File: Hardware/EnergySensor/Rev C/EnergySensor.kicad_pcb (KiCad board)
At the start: 2 copper layers, 40 parts, among them IC1 ATMEGA328P-A, J1 JACK_3POLE, P1 MAINS, P2 CONN_02X03, P3 CONN_01X12, T1 VN20.10 09477, U1 LM1084IT-3.3/NOPB, Y1 16MHz

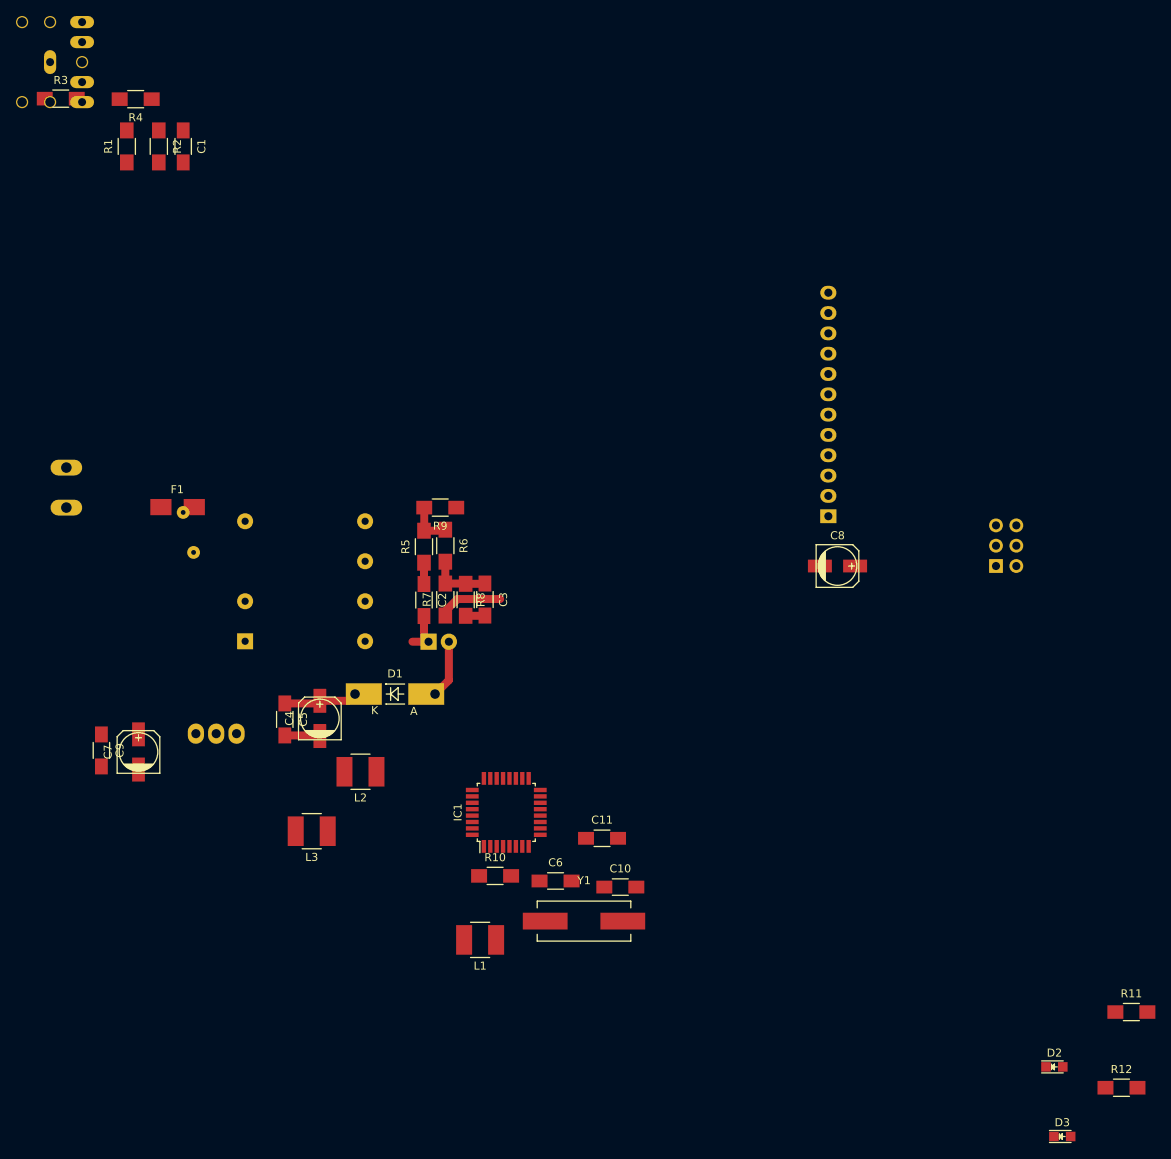
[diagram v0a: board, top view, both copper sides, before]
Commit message: moved energy sensor to nice case and various tweaks
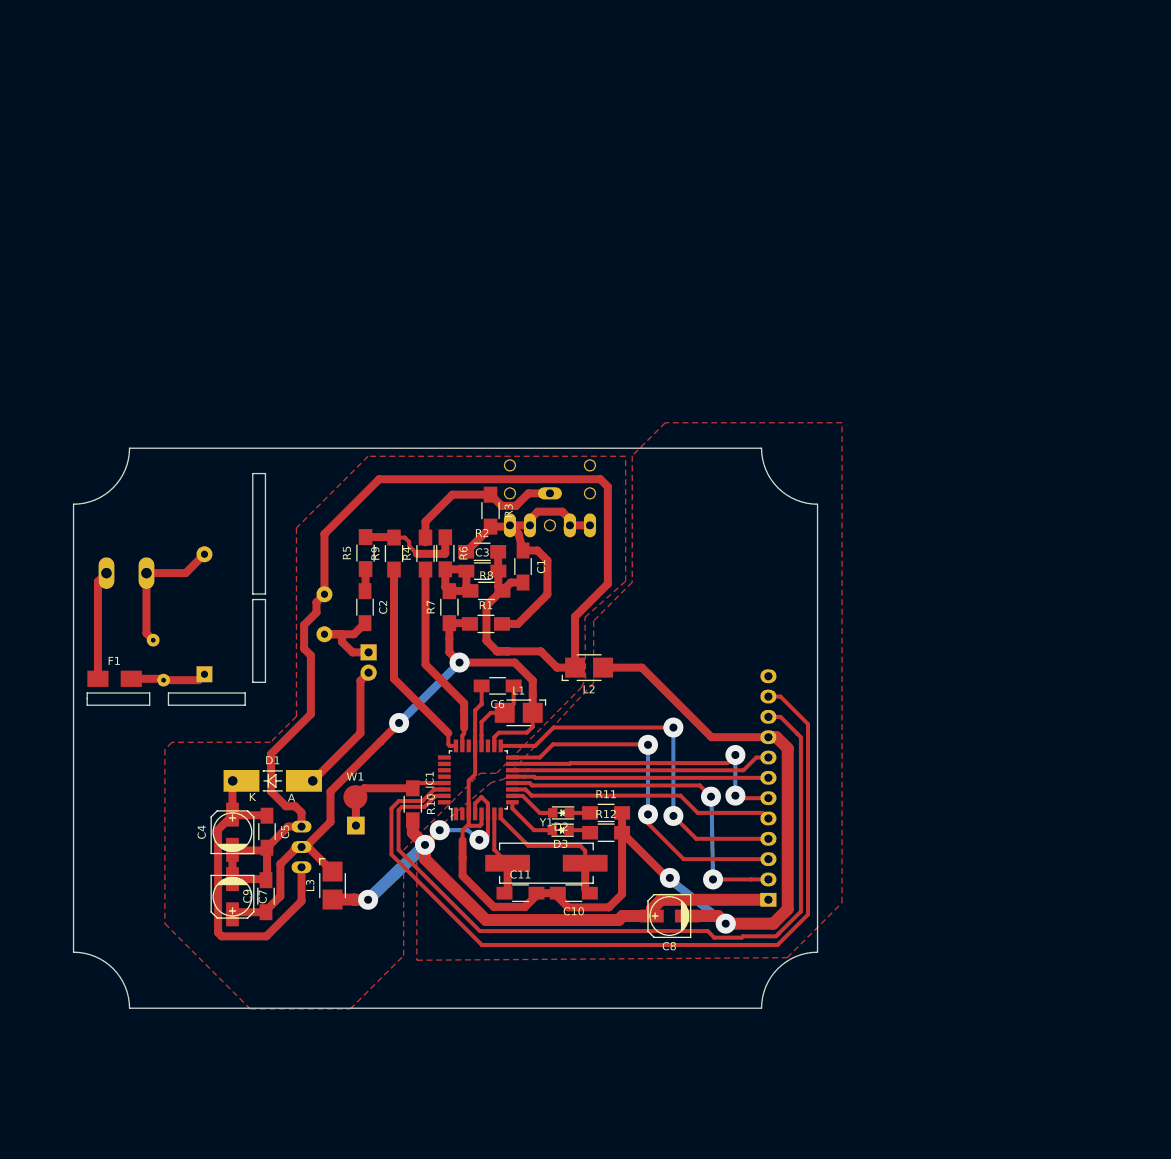
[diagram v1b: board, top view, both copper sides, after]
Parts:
- added W1: TEST_1P, Measurement_Points:Measurement_Point_Round-SMD-Pad_Big, F.Cu at (86.2, 114.6)
- L1, L2, L3: footprint Inductors:NR4018_HandSoldering -> Inductors:Inductor_1212
- P2: value CONN_02X03 -> CONN_01X01; footprint Pin_Headers:Pin_Header_Straight_2x03 -> Pin_Headers:Pin_Header_Straight_1x01
- P3: footprint Pin_Headers:Pin_Header_Angled_1x12 -> Socket_Strips:Socket_Strip_Angled_1x12
- T1: footprint Divers:TEZ-22x24 -> CustomParts:TEZ-22x24
- U1: value LM1084IT-3.3/NOPB -> ld33v; footprint TO-220 -> TO_SOT_Packages_THT:TO-220_Neutral123_Vertical
- moved P2 86.3 mm to (86.3, 118.2)
- moved R1 74.7 mm to (102.6, 93.0), turned to 0 degrees
- moved R3 74.4 mm to (103.1, 78.8), turned to 270 degrees
- moved J1 73.9 mm to (104.6, 83.1), turned to 0 degrees
- moved D3 73.5 mm to (111.9, 118.7), turned to 180 degrees
- moved R12 71.9 mm to (117.6, 119.1)
- moved R11 70.2 mm to (117.6, 116.6)
- moved D2 69.4 mm to (112.0, 116.6), turned to 180 degrees
- moved C1 67.5 mm to (107.2, 85.8)
- moved R4 67.4 mm to (95.0, 84.2), turned to 90 degrees
- moved R2 64.8 mm to (102.1, 83.9), turned to 0 degrees
- moved C8 48.5 mm to (125.5, 129.5), turned to 180 degrees
- moved P3 48.5 mm to (137.9, 127.4), turned to 90 degrees
- moved L2 31.4 mm to (115.4, 98.4)
- moved L1 28.8 mm to (106.7, 104.1), turned to 180 degrees
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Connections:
- C8 pad 1: +3.3VP -> +3V3
- C8 pad 2: GNDA -> GNDD
- P1 pad 1: Net-(P1-Pad1) -> Net-(F1-Pad1)
- P1 pad 2: Net-(F1-Pad1) -> Net-(P1-Pad2)
- P2 pad 1: /MISO -> /RESET
- T1 pad 2: Net-(P1-Pad1) -> Net-(P1-Pad2)
- VR1 pad 2: Net-(P1-Pad1) -> Net-(P1-Pad2)
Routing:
- net GNDA: track 6.84 -> 156.3 mm
- net GNDD: track 0.00 -> 142.4 mm, vias 0 -> 2
- net /RXD: track 0.00 -> 101.9 mm
- net /TXD: track 0.00 -> 94.7 mm
- net +3V3: track 0.00 -> 86.6 mm, vias 0 -> 4
- net +3.3VP: track 8.03 -> 82.7 mm, vias 0 -> 2
- net /SCK: track 0.00 -> 46.6 mm, vias 0 -> 2
- net /MISO: track 0.00 -> 44.4 mm, vias 0 -> 2
- net /CSN2: track 0.00 -> 42.8 mm, vias 0 -> 2
- net Net-(C1-Pad1): track 0.00 -> 38.5 mm
- net /MOSI: track 0.00 -> 37.7 mm, vias 0 -> 2
- net /INT: track 0.00 -> 33.5 mm
- net /CE: track 0.00 -> 32.7 mm
- net Net-(C4-Pad1): track 9.26 -> 41.4 mm
- net /CSN: track 0.00 -> 32.1 mm
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- added copper zone on F.Cu, net GNDA
- added copper zone on F.Cu, net GNDD
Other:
- board outline added: 93 x 70 mm
- net class Default: clearance 0.2 -> 0.25; trace_width 0.25 -> 0.5; via_dia 0.6 -> 2.5; via_drill 0.4 -> 1
- rule trace_clearance: 0.2 -> 0.25
- rule trace_min: 0.2 -> 0.5
- board text added: "Smart Home Energy Monitor V3 Alistair Cheeseman 2016"
